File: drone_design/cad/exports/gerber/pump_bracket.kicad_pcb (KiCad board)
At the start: 2 copper layers, 25 x 40 mm, 0 parts

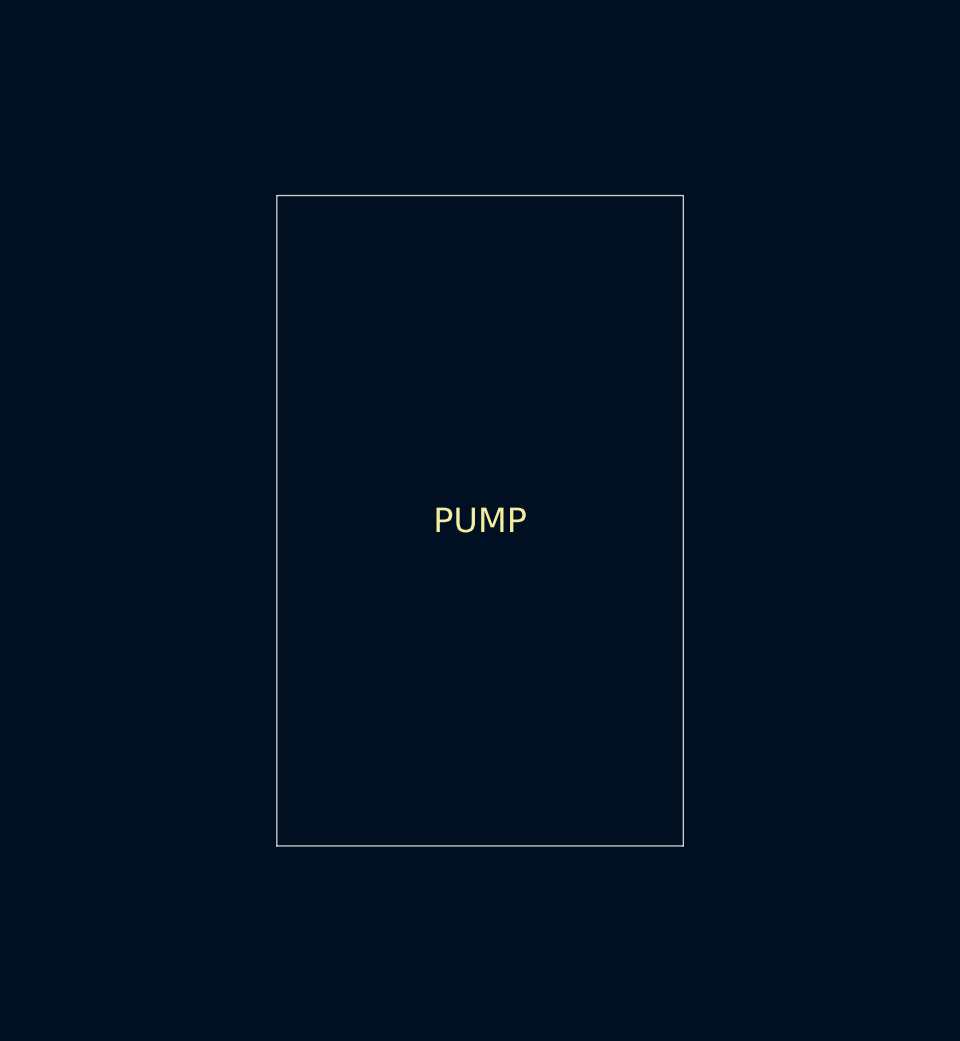
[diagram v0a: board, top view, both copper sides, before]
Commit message: feat: fix ToF bracket alignment, add motor mount to arm tips
- Fix all 6 ToF sensor/bracket positions with correct rotations
  so sensors sit flush against bracket tab faces, sensing outward
- Add circular motor mounting plate at arm tips (25mm dia)
  with 4x M2 bolt holes on 16mm circle + center shaft clearance
- Add matching M2 threaded holes to motor base plate model
- Rebuild all STLs and viewer (68 parts, 15.8 MB total)
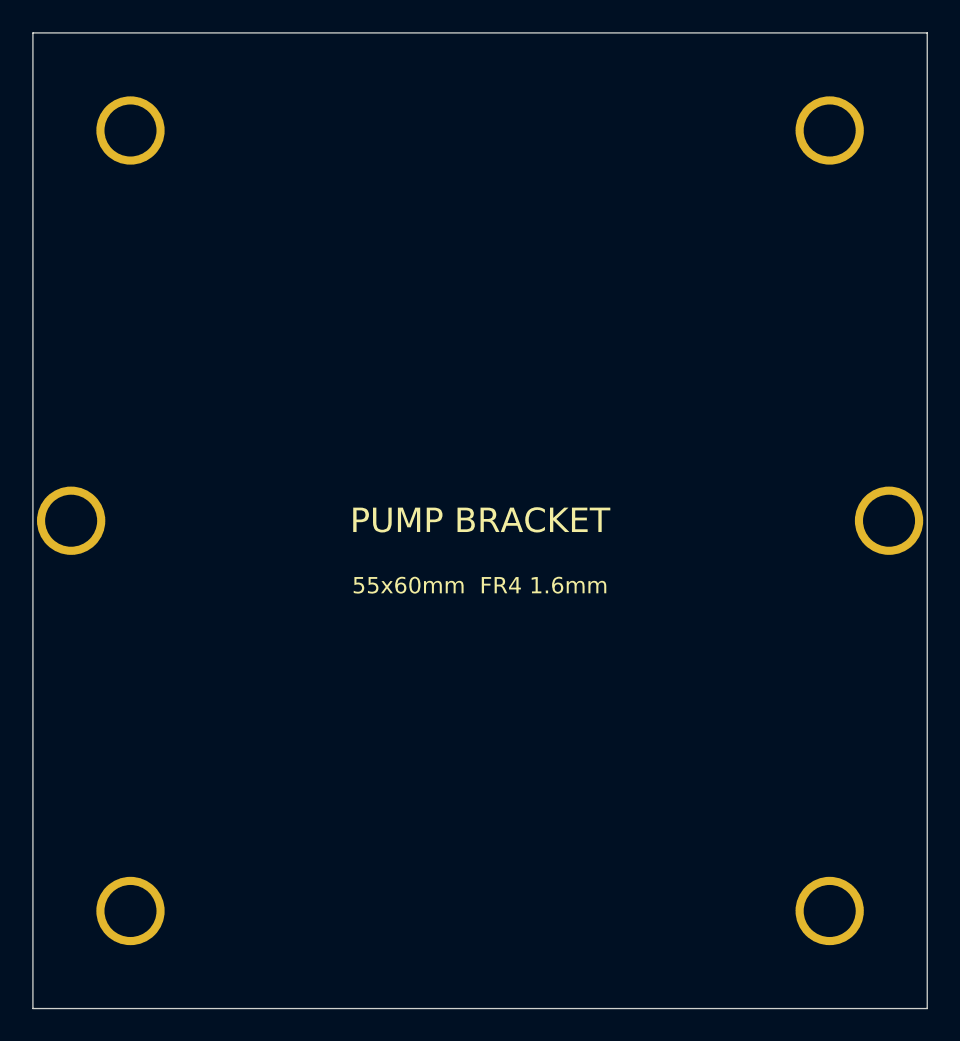
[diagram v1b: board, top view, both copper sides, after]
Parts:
- added ?: , MountingHole:MountingHole_3.2mm, F.Cu at (-21.5, -24.0)
- added ?: , MountingHole:MountingHole_3.2mm, F.Cu at (-21.5, 24.0)
- added ?: , MountingHole:MountingHole_3.2mm, F.Cu at (21.5, -24.0)
- added ?: , MountingHole:MountingHole_3.2mm, F.Cu at (21.5, 24.0)
- added ?: , MountingHole:MountingHole_3.2mm, F.Cu at (-25.1, 0.00)
- added ?: , MountingHole:MountingHole_3.2mm, F.Cu at (25.1, 0.00)
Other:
- board size 25 x 40 mm -> 55 x 60 mm
- board text added: "55x60mm FR4 1.6mm"
- board text added: "PUMP BRACKET"
- board text removed: "PUMP"
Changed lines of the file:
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@@
   )
   (net 0 "")
-  (gr_line (start -12.5000 -20.0000) (end 12.5000 -20.0000) (layer "Edge.Cuts") (width 0.05))
-  (gr_line (start 12.5000 -20.0000) (end 12.5000 20.0000) (layer "Edge.Cuts") (width 0.05))
-  (gr_line (start 12.5000 20.0000) (end -12.5000 20.0000) (layer "Edge.Cuts") (width 0.05))
-  (gr_line (start -12.5000 20.0000) (end -12.5000 -20.0000) (layer "Edge.Cuts") (width 0.05))
-  (gr_text "PUMP" (at 0.0000 0.0000) (layer "F.SilkS")
+  (gr_line (start -27.5000 -30.0000) (end 27.5000 -30.0000) (layer "Edge.Cuts") (width 0.05))
+  (gr_line (start 27.5000 -30.0000) (end 27.5000 30.0000) (layer "Edge.Cuts") (width 0.05))
+  (gr_line (start 27.5000 30.0000) (end -27.5000 30.0000) (layer "Edge.Cuts") (width 0.05))
+  (gr_line (start -27.5000 30.0000) (end -27.5000 -30.0000) (layer "Edge.Cuts") (width 0.05))
+  (footprint "MountingHole:MountingHole_3.2mm" (layer "F.Cu")
+    (at -21.5000 -24.0000)
+    (pad "" thru_hole circle (at 0 0) (size 4.20 4.20) (drill 3.20)
+      (layers "*.Cu" "*.Mask")
+    )
+  )
+  (footprint "MountingHole:MountingHole_3.2mm" (layer "F.Cu")
+    (at -21.5000 24.0000)
+    (pad "" thru_hole circle (at 0 0) (size 4.20 4.20) (drill 3.20)
+      (layers "*.Cu" "*.Mask")
+    )
+  )
+  (footprint "MountingHole:MountingHole_3.2mm" (layer "F.Cu")
+    (at 21.5000 -24.0000)
+    (pad "" thru_hole circle (at 0 0) (size 4.20 4.20) (drill 3.20)
+      (layers "*.Cu" "*.Mask")
+    )
+  )
+  (footprint "MountingHole:MountingHole_3.2mm" (layer "F.Cu")
+    (at 21.5000 24.0000)
+    (pad "" thru_hole circle (at 0 0) (size 4.20 4.20) (drill 3.20)
+      (layers "*.Cu" "*.Mask")
+    )
+  )
+  (footprint "MountingHole:MountingHole_3.2mm" (layer "F.Cu")
+    (at -25.1500 0.0000)
+    (pad "" thru_hole circle (at 0 0) (size 4.20 4.20) (drill 3.20)
+      (layers "*.Cu" "*.Mask")
+    )
+  )
+  (footprint "MountingHole:MountingHole_3.2mm" (layer "F.Cu")
+    (at 25.1500 0.0000)
+    (pad "" thru_hole circle (at 0 0) (size 4.20 4.20) (drill 3.20)
+      (layers "*.Cu" "*.Mask")
+    )
+  )
+  (gr_text "PUMP BRACKET" (at 0.0000 0.0000) (layer "F.SilkS")
     (effects (font (size 1.5 1.5) (thickness 0.15)))
   )
+  (gr_text "55x60mm  FR4 1.6mm" (at 0.0000 4.0000) (layer "F.SilkS")
+    (effects (font (size 1.0 1.0) (thickness 0.12)))
+  )
 )
